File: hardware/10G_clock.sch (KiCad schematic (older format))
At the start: 12 parts, among them U801 DIFF_OSC, U802 DIFF_OSC, U803 SI53340

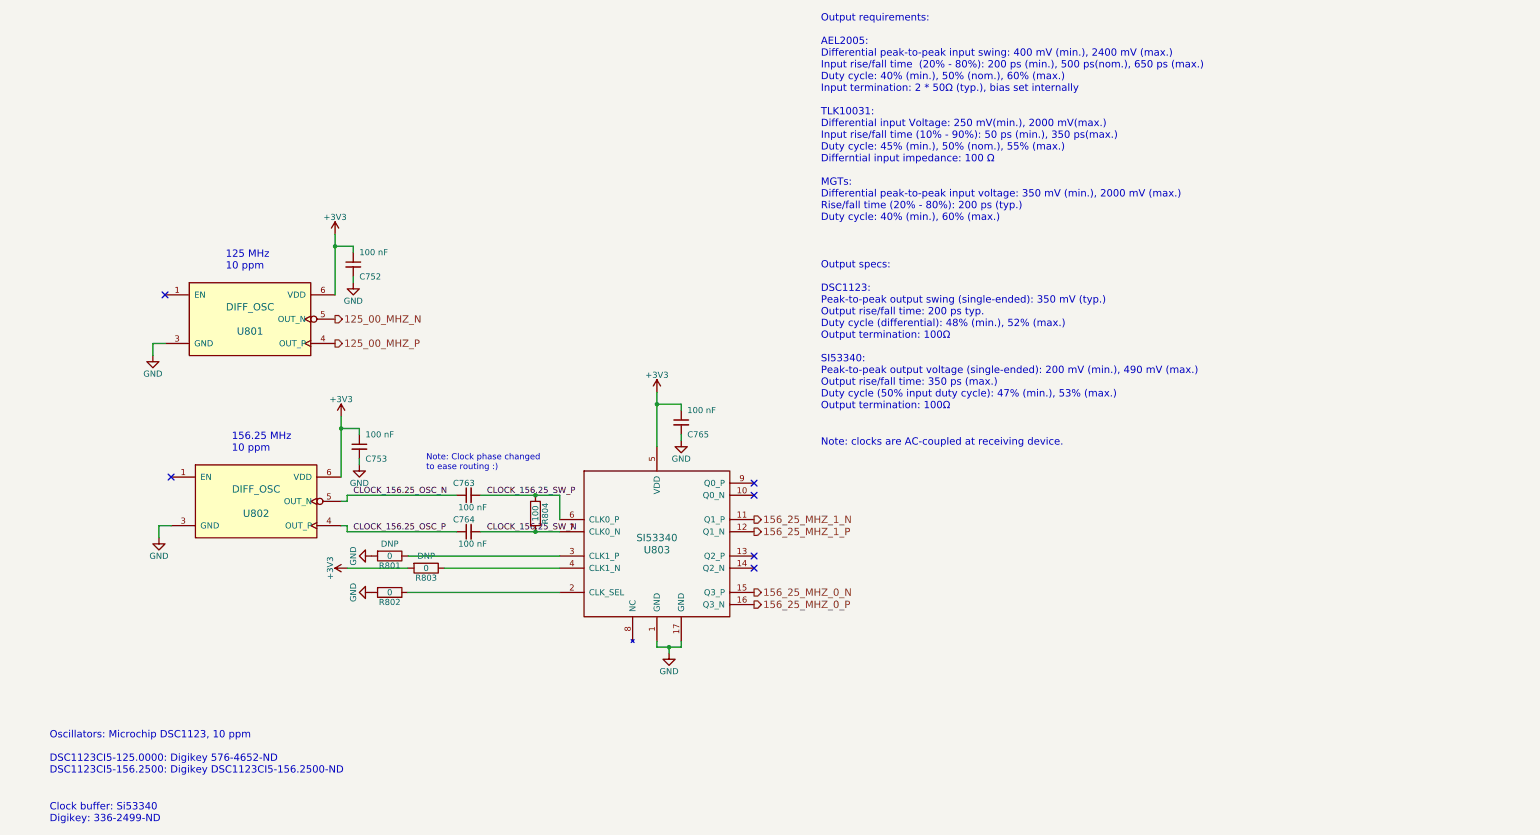
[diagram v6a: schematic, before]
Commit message: WIP: routing the HF Part of the Camera Connector. I have to move the clock away from the left border.
TODO: Fix DDR3 RAM.
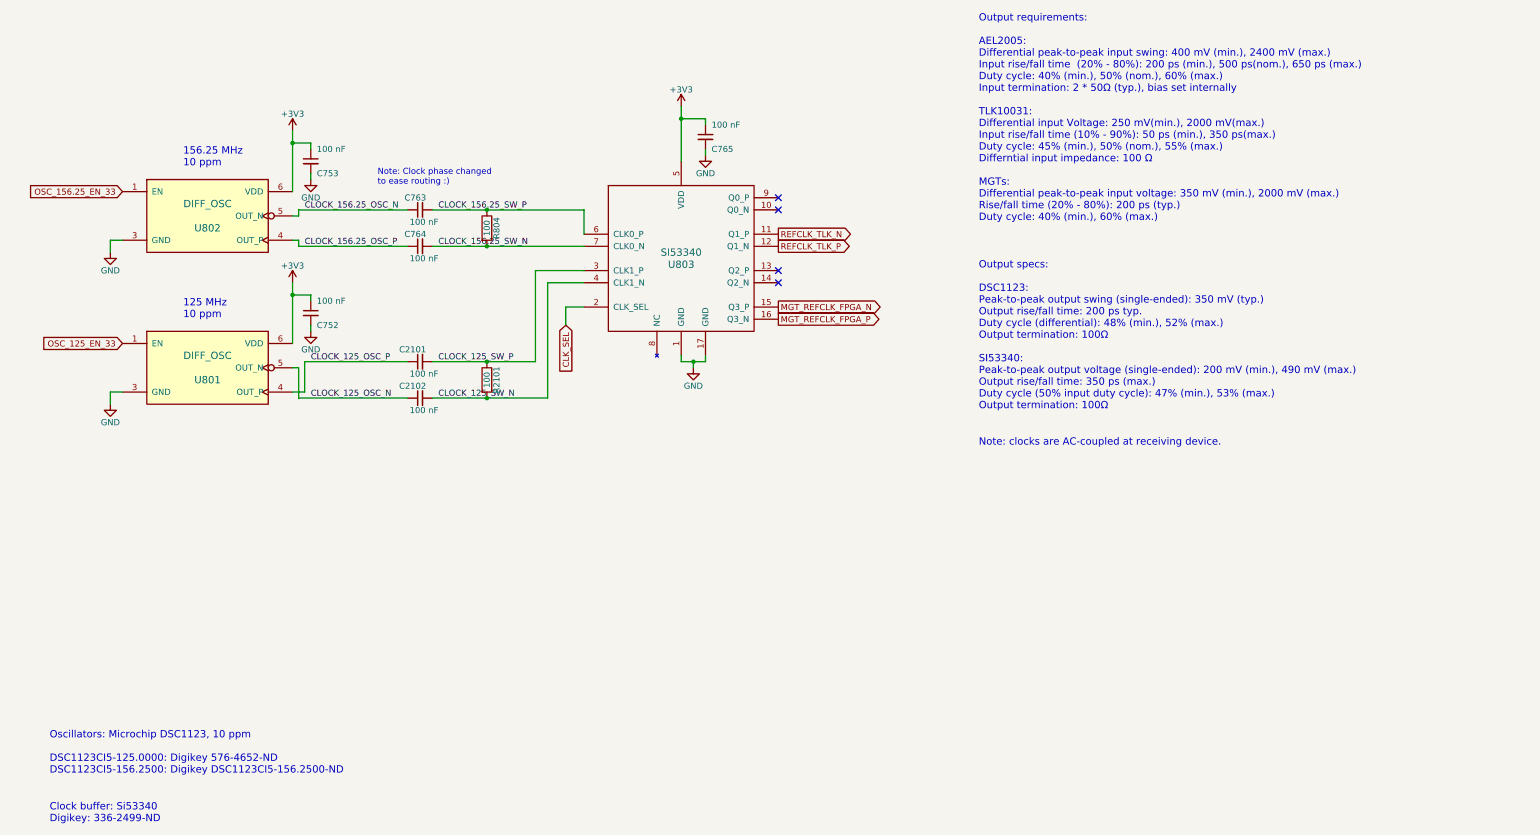
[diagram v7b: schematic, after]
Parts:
- removed R801, R802, R803: 0, Resistor_SMD:R_0402_1005Metric, symbol Device:R
- added C2101, C2102: 100 nF, Capacitor_SMD:C_0201_0603Metric, symbol Device:C_Small
- added R2101: 100, Resistor_SMD:R_0402_1005Metric, symbol Device:R
- U803: Populate for CLG484(Z-7012s/Z-7015) (none) -> 1; Populate for SBGA485(Z-7030) (none) -> 1
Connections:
- net OSC_125_EN_33: now reaches U801.1 (EN)
- net OSC_156.25_EN_33: now reaches U802.1 (EN)
- net CLK_SEL: now reaches U803.2 (CLK_SEL)
- net CLOCK_125_SW_P: now reaches U803.3 (CLK1_P)
- net CLOCK_125_SW_P: now also C2101.2, R2101.1
- net CLOCK_125_SW_N: now reaches U803.4 (CLK1_N)
- net CLOCK_125_SW_N: now also C2102.2, R2101.2
- net 125_00_MHZ_N renamed CLOCK_125_OSC_N
- net CLOCK_125_OSC_N: now also C2102.1
- net 125_00_MHZ_P renamed CLOCK_125_OSC_P
- net CLOCK_125_OSC_P: now also C2101.1
- net 156_25_MHZ_0_N renamed MGT_REFCLK_FPGA_N
- net 156_25_MHZ_0_P renamed MGT_REFCLK_FPGA_P
- net 156_25_MHZ_1_N renamed REFCLK_TLK_N
- net 156_25_MHZ_1_P renamed REFCLK_TLK_P
- no-connect marks 6 -> 4
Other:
- moved on the sheet: C752, C753, C763, C764, C765, R804, U801, U802, U803

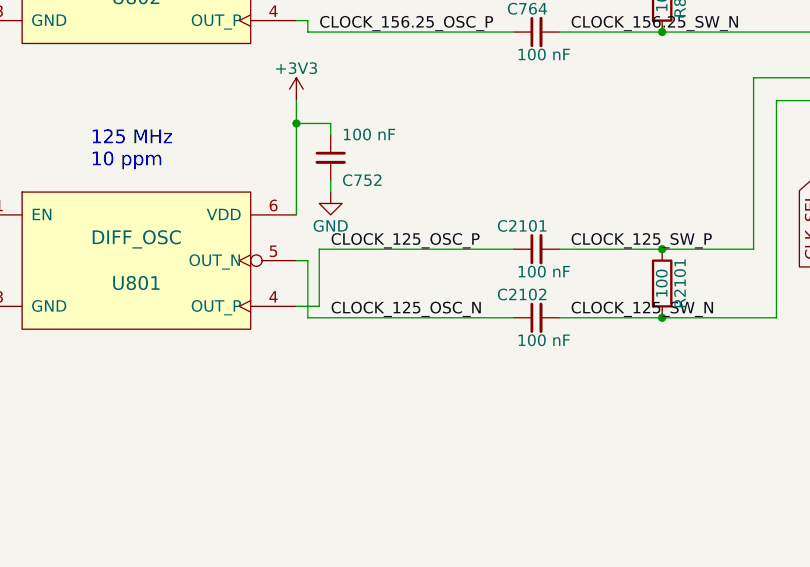
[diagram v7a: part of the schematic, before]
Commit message: Routed a first Version of the High Speed Part of the Camera Connector. The optional LVDS Clocks are left unconnected. I couldn't keep the Connectors Pin Assignment because it was just impossible to route.
WIP: general Routing

Fixed: DDR3 Trace Length Matching
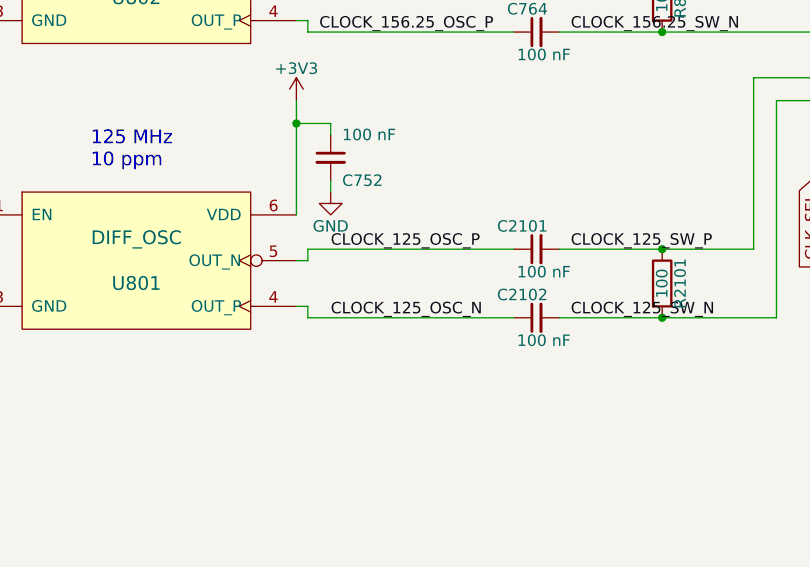
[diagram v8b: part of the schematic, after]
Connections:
- net CLOCK_125_OSC_N: now also U801.4 (OUT_P); no longer U801.5 (OUT_N)
- net CLOCK_125_OSC_P: now also U801.5 (OUT_N); no longer U801.4 (OUT_P)
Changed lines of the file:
@@
 	5000 3150 5000 3000
 Wire Wire Line
-	2750 3700 2850 3700
+	2750 3500 2800 3500
 Wire Wire Line
-	2850 3700 2850 3450
+	2800 3500 2800 3450
 Wire Wire Line
-	2850 3450 3700 3450
+	2800 3450 3700 3450
 Wire Wire Line
-	2800 3750 2800 3500
+	2750 3700 2800 3700
 Wire Wire Line
-	2800 3500 2750 3500
+	2800 3700 2800 3750
 $EndSCHEMATC
